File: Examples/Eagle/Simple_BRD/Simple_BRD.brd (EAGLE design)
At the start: 82.5 x 67.3 mm, 58 parts

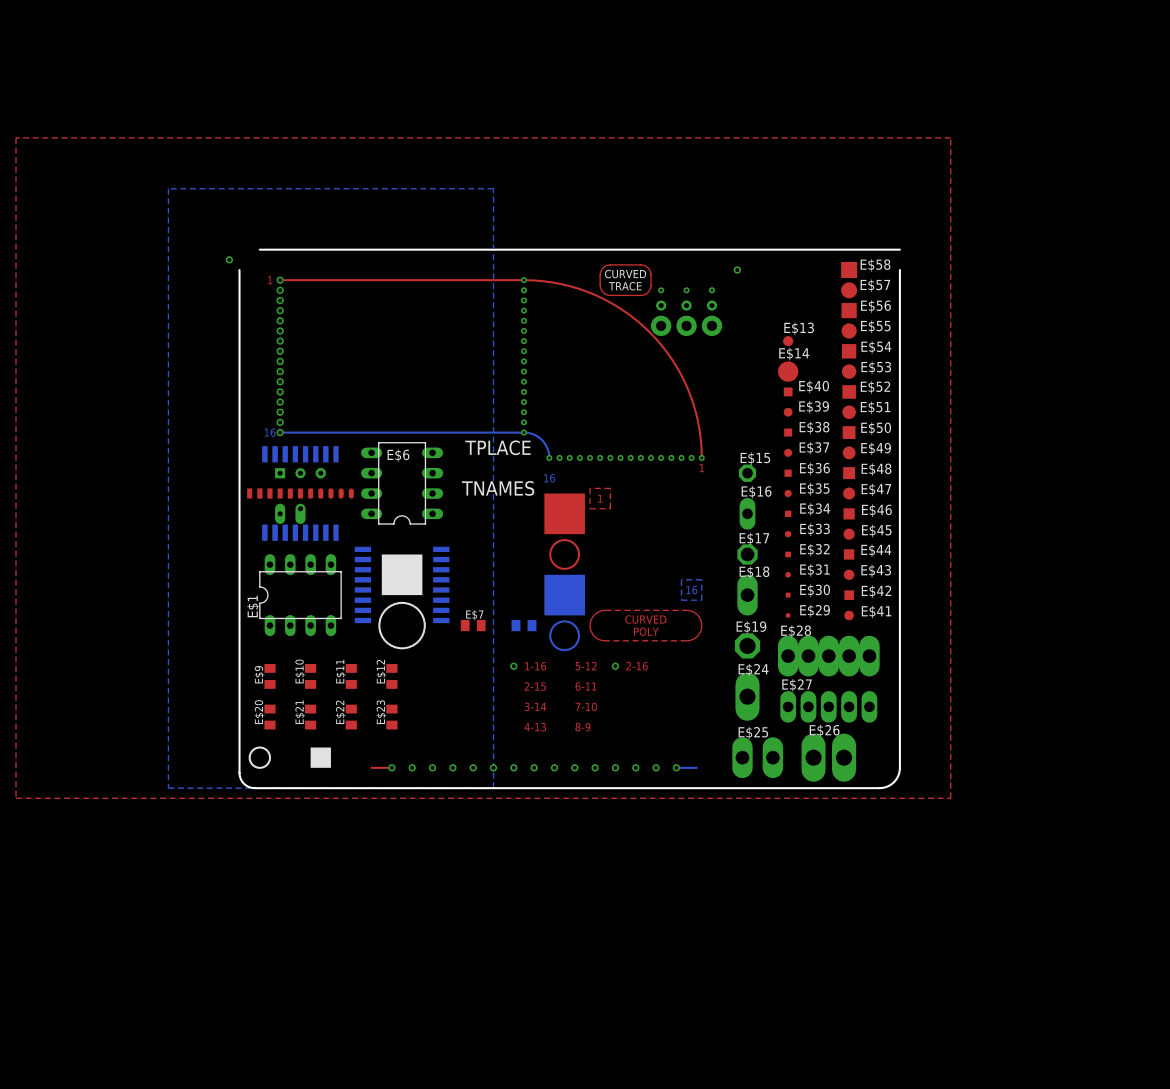
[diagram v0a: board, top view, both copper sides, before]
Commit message: Modified PCB to layout items to make PCB validation easier.
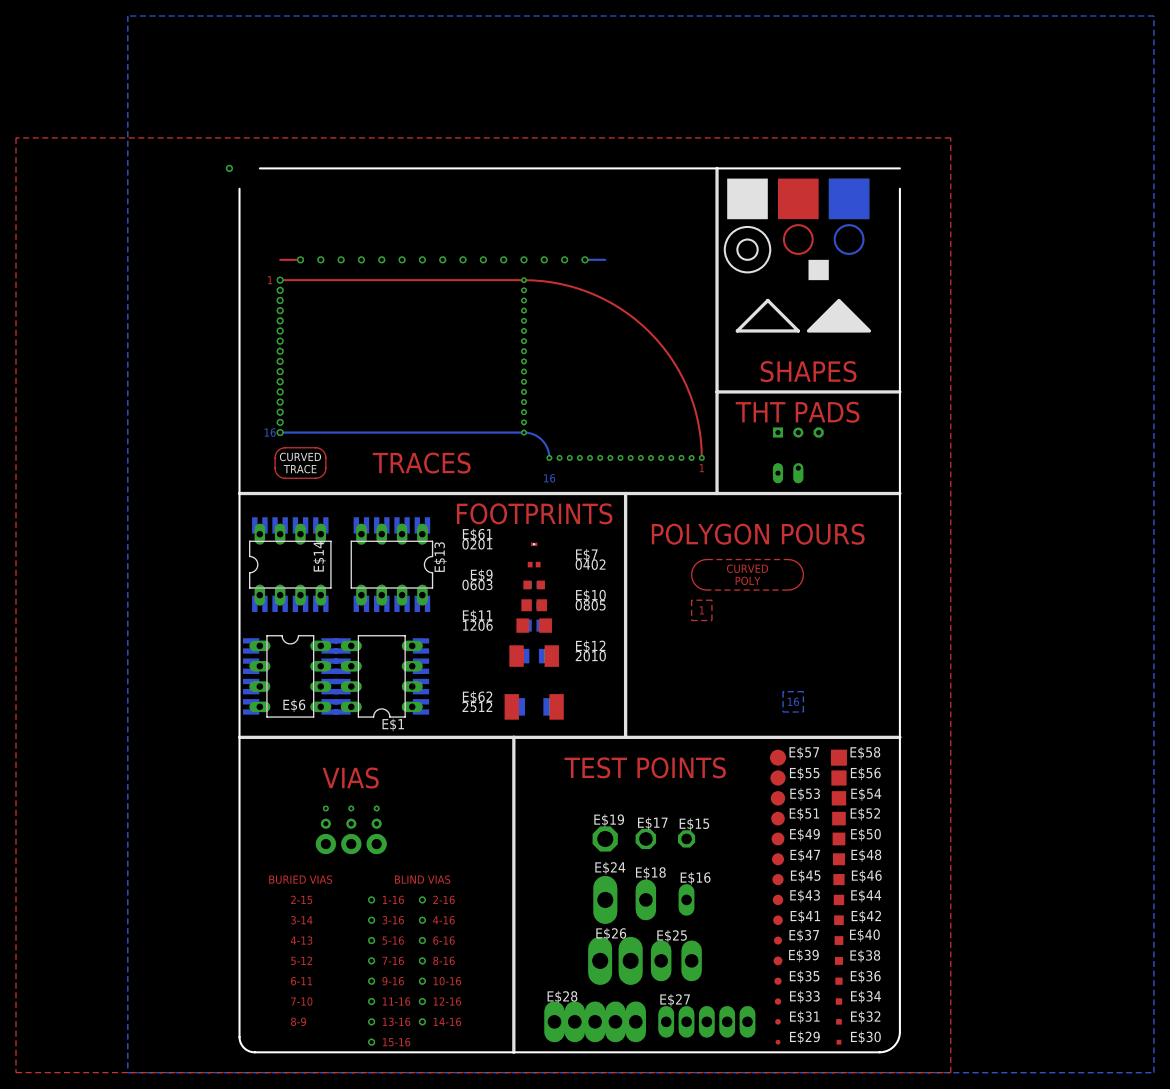
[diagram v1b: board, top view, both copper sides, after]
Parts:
- removed E$4: (no value), untitled:TEST2
- removed E$8: 1uF, adafruit:C0805K
- added E$59, E$60: (no value), 74xx-us:SO16L
- added E$61: 0R, rcl:R0201
- added E$62: 6R, rcl:R2512
- added E$63: 5C, rcl:C1808
- E$10: value 10uF -> 3R; device adafruit:C0805K -> rcl:R0805
- E$11: value 10uF -> 4R; device adafruit:C0805K -> rcl:R1206
- E$12: value 10uF -> 5R; device adafruit:C0805K -> rcl:R2010
- E$13: device testpad:B1,27 -> 74xx-us:DIL08
- E$14: device testpad:B2,54 -> 74xx-us:DIL08
- E$20: value 10uF -> 0C; device adafruit:C0805K -> rcl:C0402
- E$21: value 10uF -> 2C; device adafruit:C0805K -> rcl:C0603
- E$22: value 10uF -> 3C; device adafruit:C0805K -> rcl:C0805
- E$23: value 10uF -> 4C; device adafruit:C0805K -> rcl:C1206
- E$7: value 1uF -> 1R; device adafruit:C0805K -> rcl:R0402
- E$9: value 10uF -> 2R; device adafruit:C0805K -> rcl:R0603
- moved E$40 68.9 mm to (74.9, -33.0)
- moved E$39 68.6 mm to (67.3, -35.6)
- moved E$14 66.7 mm to (6.35, 14.0)
- moved E$38 66.3 mm to (74.9, -35.6)
- moved E$36 63.8 mm to (74.9, -38.1)
- moved E$3 62.4 mm to (67.3, 30.5)
- moved E$34 61.3 mm to (74.9, -40.6)
- moved E$37 61.0 mm to (67.3, -33.0)
- moved E$35 61.0 mm to (67.3, -38.1)
- moved E$58 61.0 mm to (74.9, -10.2)
- moved E$57 59.1 mm to (67.3, -10.2)
- moved E$32 58.8 mm to (74.9, -43.2)
- moved E$33 58.4 mm to (67.3, -40.6)
- moved E$56 58.4 mm to (74.9, -12.7)
- moved E$13 56.9 mm to (19.1, 14.0), turned to 180 degrees
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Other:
- board size 82.5 x 67.3 mm -> 82.5 x 110.5 mm
- board text added: "0201"
- board text added: "0402"
- board text added: "0603"
- board text added: "0805"
- board text added: "10-16"
- board text added: "11-16"
- board text added: "12-16"
- board text added: "1206"
- board text added: "13-16"
- board text added: "14-16"
- board text added: "15-16"
- board text added: "1808"
- board text added: "2010"
- board text added: "2512"
- board text added: "3-16"
- board text added: "4-16"
- board text added: "5-16"
- board text added: "6-16"
- board text added: "7-16"
- board text added: "8-16"
- board text added: "9-16"
- board text added: "BLIND VIAS"
- board text added: "BURIED VIAS"
- board text added: "FOOTPRINTS"
- board text added: "POLYGON POURS"
- board text added: "SHAPES"
- board text added: "TEST POINTS"
- board text added: "THT PADS"
- board text added: "TRACES"
- board text added: "VIAS"
- board text removed: "BDOC"
- board text removed: "BNAMES"
- board text removed: "BPLACE"
- board text removed: "BVALUES"
- board text removed: "TDOC"
- board text removed: "TNAMES"
- board text removed: "TPLACE"
- board text removed: "TVALUES"

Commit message: Created better method for calculating part bounding box.
Bounding boxes in EagleCAD can be defined with UL_Area, but this also includes
exploded text location for part with the bounding box of UL_AREA.

Now looking at the pins position and pin size, a bounding box is derived from
this information.

Closes #61
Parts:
- moved E$26 2.54 mm to (44.5, -35.6), turned to 90 degrees
- moved E$24 1.27 mm to (44.5, -27.9), turned to 90 degrees
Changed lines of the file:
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@@
 <drawing>
 <settings>
-<setting alwaysvectorfont="yes"/>
+<setting alwaysvectorfont="no"/>
 <setting verticaltext="up"/>
 </settings>
@@
 <element name="E$3" library="untitled" package="TEST" value="" x="67.31" y="30.48" smashed="yes"/>
 <element name="E$5" library="74xx-us" library_urn="urn:adsk.eagle:library:88" package="SO16L" package3d_urn="urn:adsk.eagle:package:17518/1" value="" x="19.05" y="13.97" smashed="yes" rot="MR0">
-<attribute name="NAME" x="24.638" y="10.414" size="1.27" layer="26" ratio="10" rot="MR90"/>
+<attribute name="NAME" x="84.328" y="-45.466" size="1.27" layer="26" ratio="10" rot="MR90"/>
 <attribute name="VALUE" x="22.606" y="13.208" size="1.27" layer="28" ratio="10" rot="MR0"/>
 </element>
@@
 <attribute name="VALUE" x="45.72" y="-20.32" size="0.0254" layer="27"/>
 </element>
-<element name="E$24" library="testpad" library_urn="urn:adsk.eagle:library:385" package="P1-20Y" package3d_urn="urn:adsk.eagle:package:27951/1" value="" x="45.72" y="-27.94" smashed="yes">
-<attribute name="NAME" x="44.323" y="-24.511" size="1.27" layer="25" ratio="10"/>
-<attribute name="VALUE" x="45.72" y="-27.94" size="0.0254" layer="27"/>
+<element name="E$24" library="testpad" library_urn="urn:adsk.eagle:library:385" package="P1-20Y" package3d_urn="urn:adsk.eagle:package:27951/1" value="" x="44.45" y="-27.94" smashed="yes" rot="R90">
+<attribute name="NAME" x="41.021" y="-29.337" size="1.27" layer="25" ratio="10" rot="R90"/>
+<attribute name="VALUE" x="44.45" y="-27.94" size="0.0254" layer="27" rot="R90"/>
 </element>
 <element name="E$25" library="testpad" library_urn="urn:adsk.eagle:library:385" package="P2-38-17" package3d_urn="urn:adsk.eagle:package:27945/1" value="" x="54.61" y="-35.56" smashed="yes">
@@
 <attribute name="VALUE" x="52.07" y="-39.37" size="1.27" layer="27" ratio="10"/>
 </element>
-<element name="E$26" library="testpad" library_urn="urn:adsk.eagle:library:385" package="P2-38-20" package3d_urn="urn:adsk.eagle:package:27982/1" value="" x="46.99" y="-35.56" smashed="yes">
-<attribute name="NAME" x="44.45" y="-32.766" size="1.27" layer="25" ratio="10"/>
-<attribute name="VALUE" x="44.45" y="-39.751" size="1.27" layer="27" ratio="10"/>
+<element name="E$26" library="testpad" library_urn="urn:adsk.eagle:library:385" package="P2-38-20" package3d_urn="urn:adsk.eagle:package:27982/1" value="" x="44.45" y="-35.56" smashed="yes" rot="R90">
+<attribute name="NAME" x="41.656" y="-38.1" size="1.27" layer="25" ratio="10" rot="R90"/>
+<attribute name="VALUE" x="48.641" y="-38.1" size="1.27" layer="27" ratio="10" rot="R90"/>
 </element>
 <element name="E$27" library="testpad" library_urn="urn:adsk.eagle:library:385" package="P5-25-13" package3d_urn="urn:adsk.eagle:package:27983/1" value="" x="58.42" y="-43.18" smashed="yes">
@@
 </element>
 <element name="E$13" library="74xx-us" library_urn="urn:adsk.eagle:library:88" package="DIL08" package3d_urn="urn:adsk.eagle:package:29519/2" value="" x="19.05" y="13.97" smashed="yes" rot="R180">
-<attribute name="NAME" x="24.384" y="16.891" size="1.27" layer="25" ratio="10" rot="R270"/>
+<attribute name="NAME" x="-9.906" y="66.421" size="1.27" layer="25" ratio="10" rot="R270"/>
 <attribute name="VALUE" x="22.606" y="14.605" size="1.27" layer="27" ratio="10" rot="R180"/>
 </element>

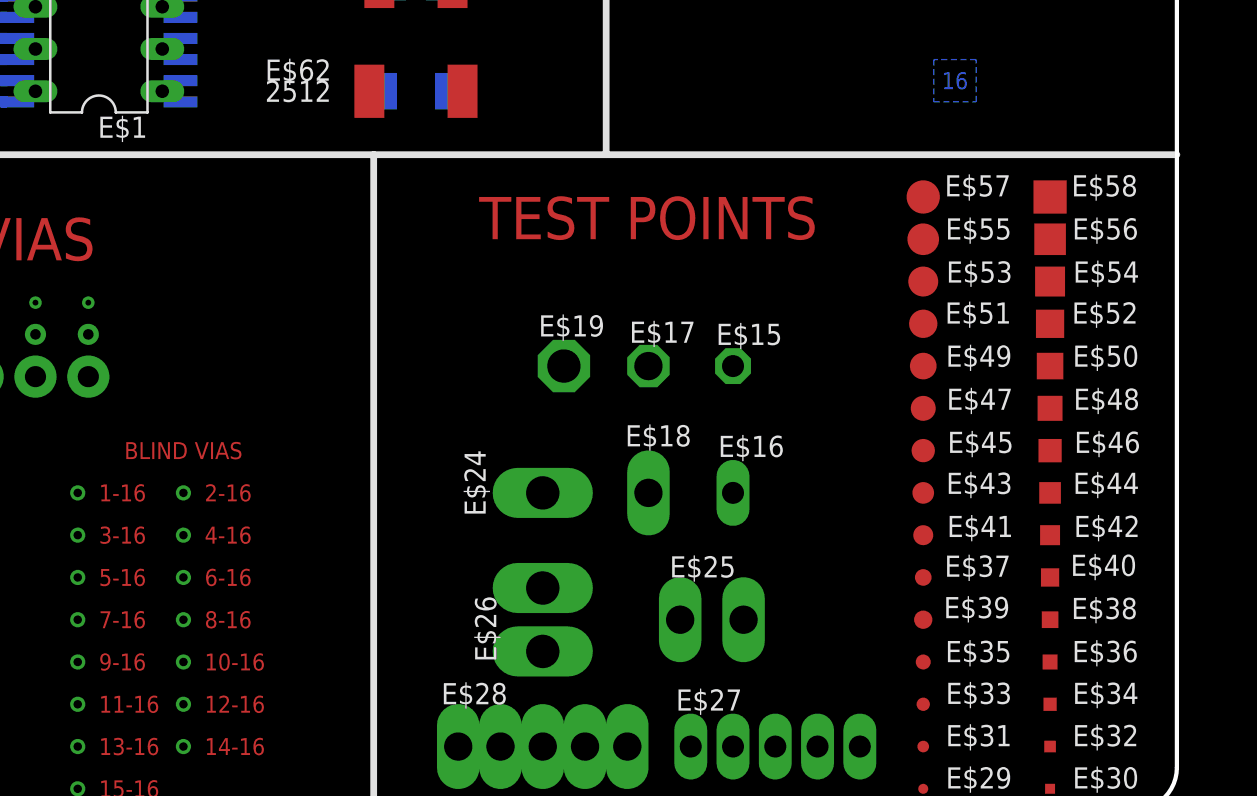
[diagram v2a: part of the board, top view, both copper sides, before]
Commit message: Updated bounding boxes to rotate around part
Bounding boxes were simple rectangles. Modified bounding box rectangles
to rotate if part being covered is rotated.
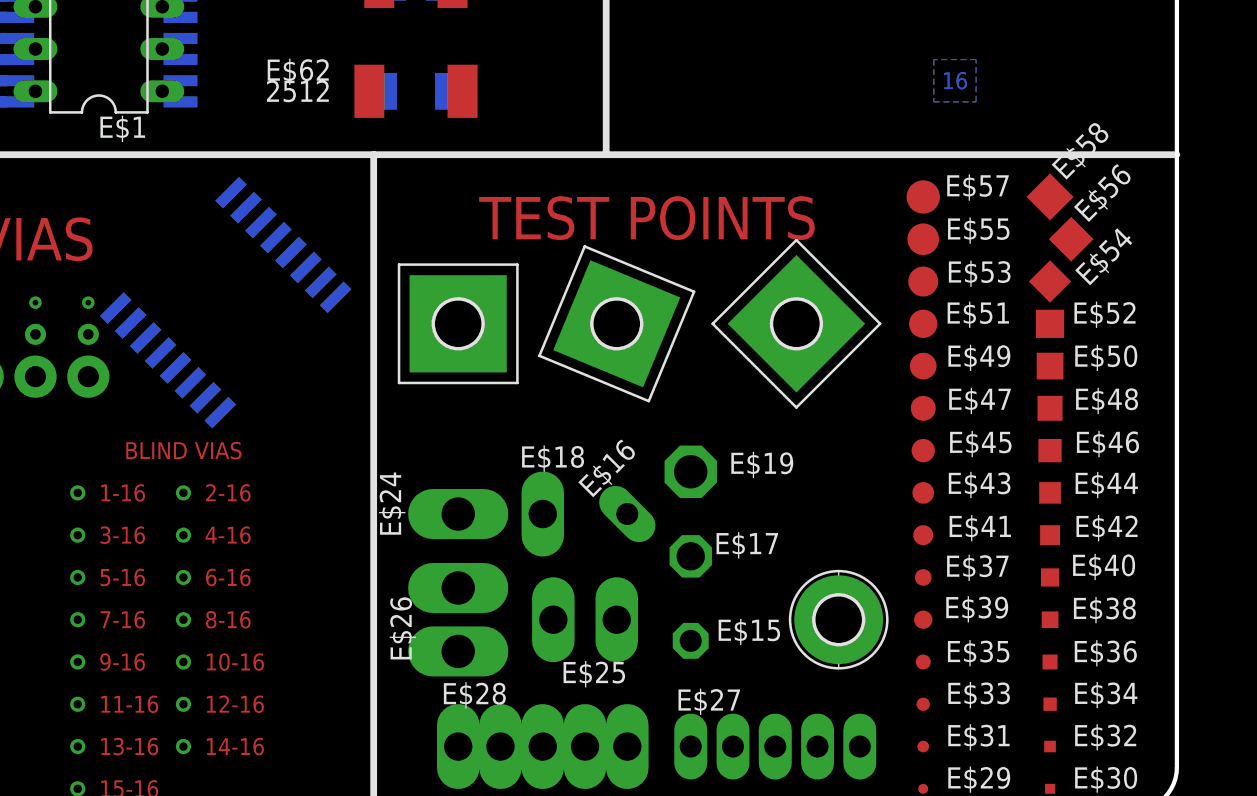
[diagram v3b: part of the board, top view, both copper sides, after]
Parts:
- added E$4, E$64, E$65: (no value), holes:2,8-PAD-SQUARE
- added E$66: (no value), 74xx-us:SO16L
- added E$8: (no value), holes:2,8-PAD
- moved E$15 16.7 mm to (53.3, -36.8), turned to 270 degrees
- moved E$17 11.7 mm to (53.3, -31.8), turned to 270 degrees
- moved E$19 9.92 mm to (53.3, -26.7), turned to 270 degrees
- moved E$25 7.62 mm to (47.0, -35.6), turned to 180 degrees
- moved E$16 6.48 mm to (49.5, -29.2), turned to 45 degrees
- moved E$18 6.48 mm to (44.5, -29.2)
- moved E$24 5.24 mm to (39.4, -29.2)
- moved E$26 5.08 mm to (39.4, -35.6)
- moved E$56 1.27 mm to (76.2, -12.7), turned to 45 degrees
- turned E$54 to 45 degrees
- turned E$58 to 45 degrees
